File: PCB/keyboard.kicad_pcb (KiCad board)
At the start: 2 copper layers, 314.3 x 95.2 mm, 153 parts, among them J1 JST SH 4-pin, SW1 SW_Push, U1 ATmega32U4-A, U2 SRV05-4, Y1 16MHz

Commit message: Finished PCB designed, still not tested
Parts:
- added G***: LOGO, LOGO, F.Cu at (158.0, 316.7)
- added G***: LOGO, LOGO, F.Cu at (206.4, 315.9)
- moved C3 0.87 mm to (351.7, 268.5)
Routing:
- net GND: track 97.4 -> 132.0 mm
- net COL0: track 412.1 -> 416.8 mm
- net COL14: track 41.2 -> 43.5 mm
- net COL2: track 375.7 -> 377.1 mm
- net Net-(U1-XTAL1): track 9.71 -> 8.84 mm
- net D+: track 14.0 -> 13.4 mm
- net COL1: track 399.5 -> 399.4 mm, vias 2 -> 4
- net COL5: track 286.5 -> 286.4 mm, vias 2 -> 4
- added copper zone on B.Cu, net GND
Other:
- board text added: "1"
- board text added: "11.26.2022"
- board text added: "Designed by GAN!A"
- board text added: "Early, not yet tested version 0.1"
- board text added: "WD66 1st batch proto"
- board text added: "WD66 by 11Customs"

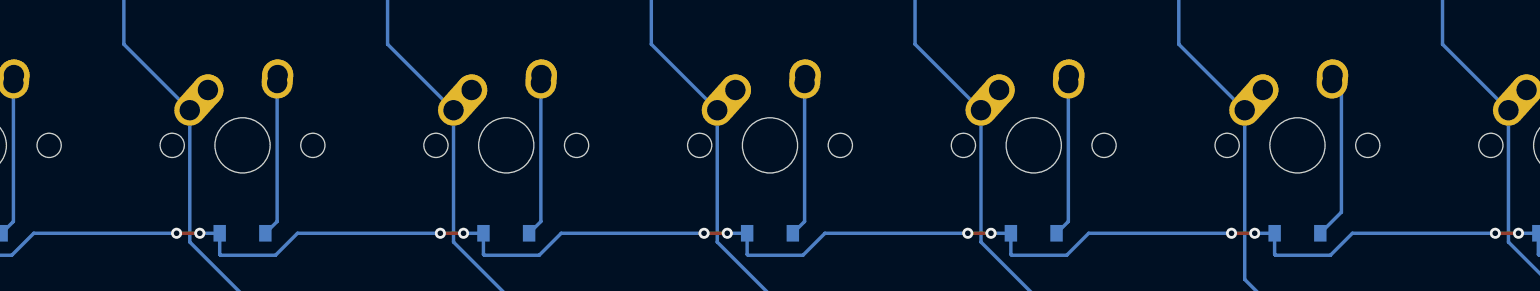
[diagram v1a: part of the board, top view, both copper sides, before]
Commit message: added holes for center standoffs
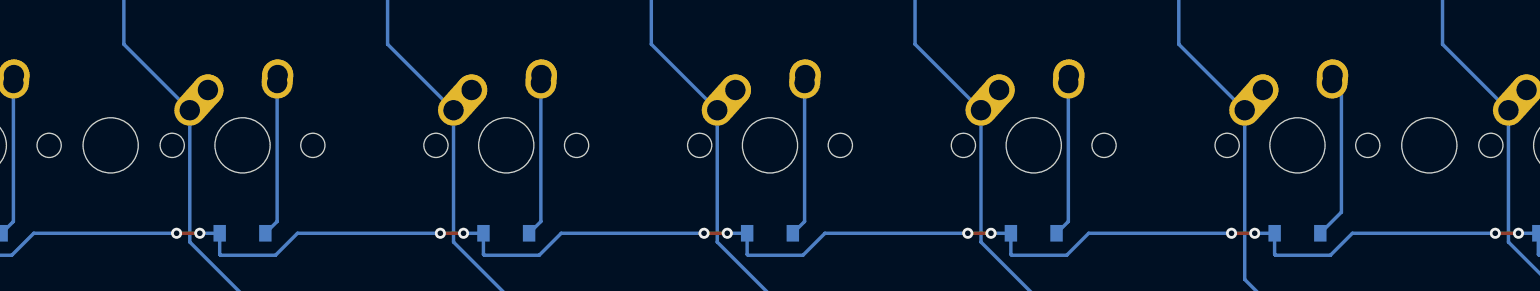
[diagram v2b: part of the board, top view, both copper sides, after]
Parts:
- added ?: , , F.Cu at (169.1, 278.6)
- added ?: , , F.Cu at (264.3, 278.6)
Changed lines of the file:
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@@
       (stroke (width 0.15) (type solid)) (layer "Dwgs.User"))
     (pad "" np_thru_hole circle locked (at -5.08 0 48.0996) (size 1.75 1.75) (drill 1.75) (layers *.Cu *.Mask))
-    (pad "" np_thru_hole circle locked (at 0 0) (size 3.9878 3.9878) (drill 3.9878) (layers *.Cu *.Mask))
+    (pad "" np_thru_hole circle locked (at 0 0) (size 3.9878 3.9878) (drill 3.9878) (layers F&B.Cu *.Mask))
     (pad "" np_thru_hole circle locked (at 5.08 0 48.0996) (size 1.75 1.75) (drill 1.75) (layers *.Cu *.Mask))
     (pad "1" thru_hole oval locked (at -3.81 -2.54 48.0996) (size 4.211556 2.25) (drill 1.47 (offset 0.980778 0)) (layers *.Cu "B.Mask")
@@
     (pad "2" thru_hole circle locked (at 2.54 -5.08) (size 2.25 2.25) (drill 1.47) (layers *.Cu "B.Mask")
       (net 48 "Net-(D28-A)") (pinfunction "ROW") (pintype "passive"))
+  )
+  (footprint "" (layer "F.Cu")
+    (at 169.06875 278.60625)
+    (fp_text reference "" (at 0 0) (layer "F.SilkS")
+      (effects (font (size 1.27 1.27) (thickness 0.15)))
+    )
+    (fp_text value "" (at 0 0) (layer "F.SilkS")
+      (effects (font (size 1.27 1.27) (thickness 0.15)))
+    )
+    (pad "" np_thru_hole circle locked (at 0 0) (size 3.9878 3.9878) (drill 3.9878) (layers F&B.Cu *.Mask))
   )
   (footprint "MX_Alps_Hybrid:MX-1U-NoLED" (layer "F.Cu")
@@
       (net 70 "Net-(D50-A)") (pinfunction "ROW") (pintype "passive"))
   )
+  (footprint "" (layer "F.Cu")
+    (at 264.31875 278.60625)
+    (fp_text reference "" (at 0 0) (layer "F.SilkS")
+      (effects (font (size 1.27 1.27) (thickness 0.15)))
+    )
+    (fp_text value "" (at 0 0) (layer "F.SilkS")
+      (effects (font (size 1.27 1.27) (thickness 0.15)))
+    )
+    (pad "" np_thru_hole circle locked (at 0 0) (size 3.9878 3.9878) (drill 3.9878) (layers F&B.Cu *.Mask))
+  )
   (footprint "MX_Alps_Hybrid:MX-1.5U-NoLED" (layer "F.Cu")

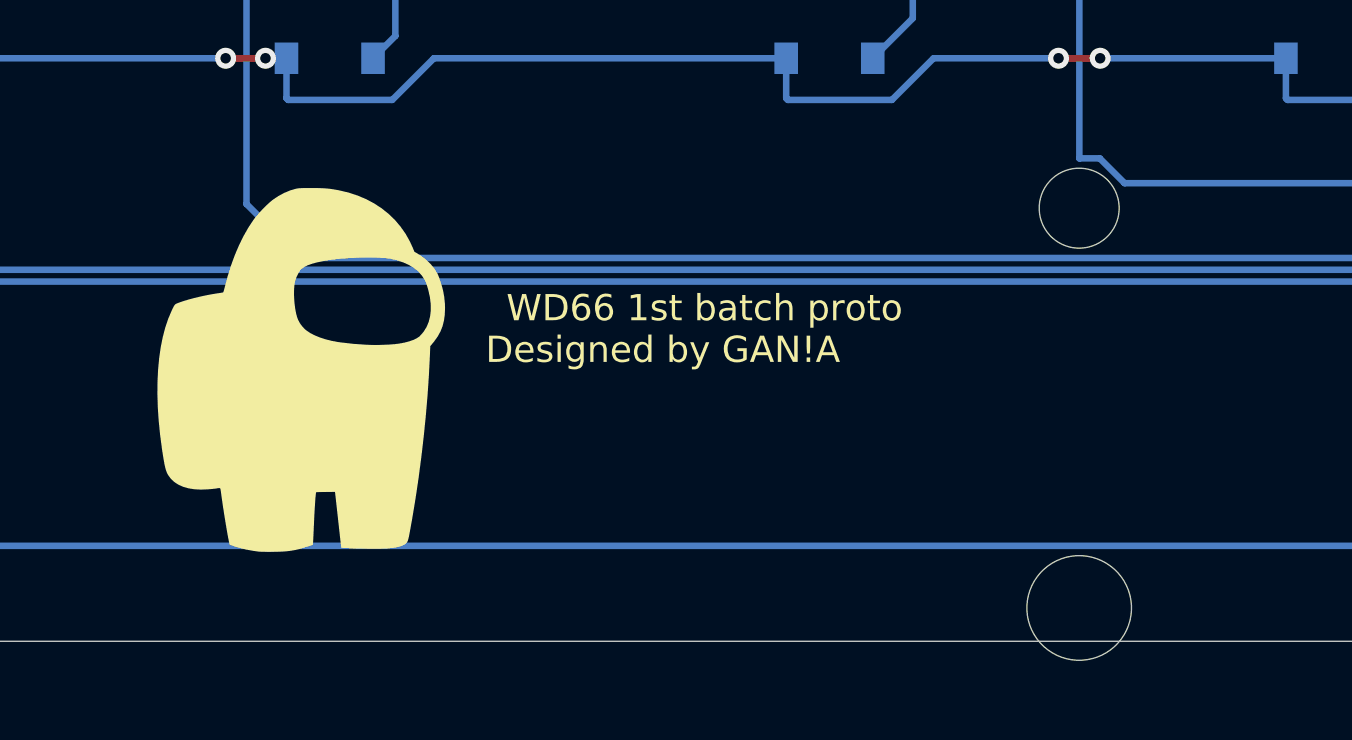
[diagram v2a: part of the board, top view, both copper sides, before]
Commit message: updated silkscreen
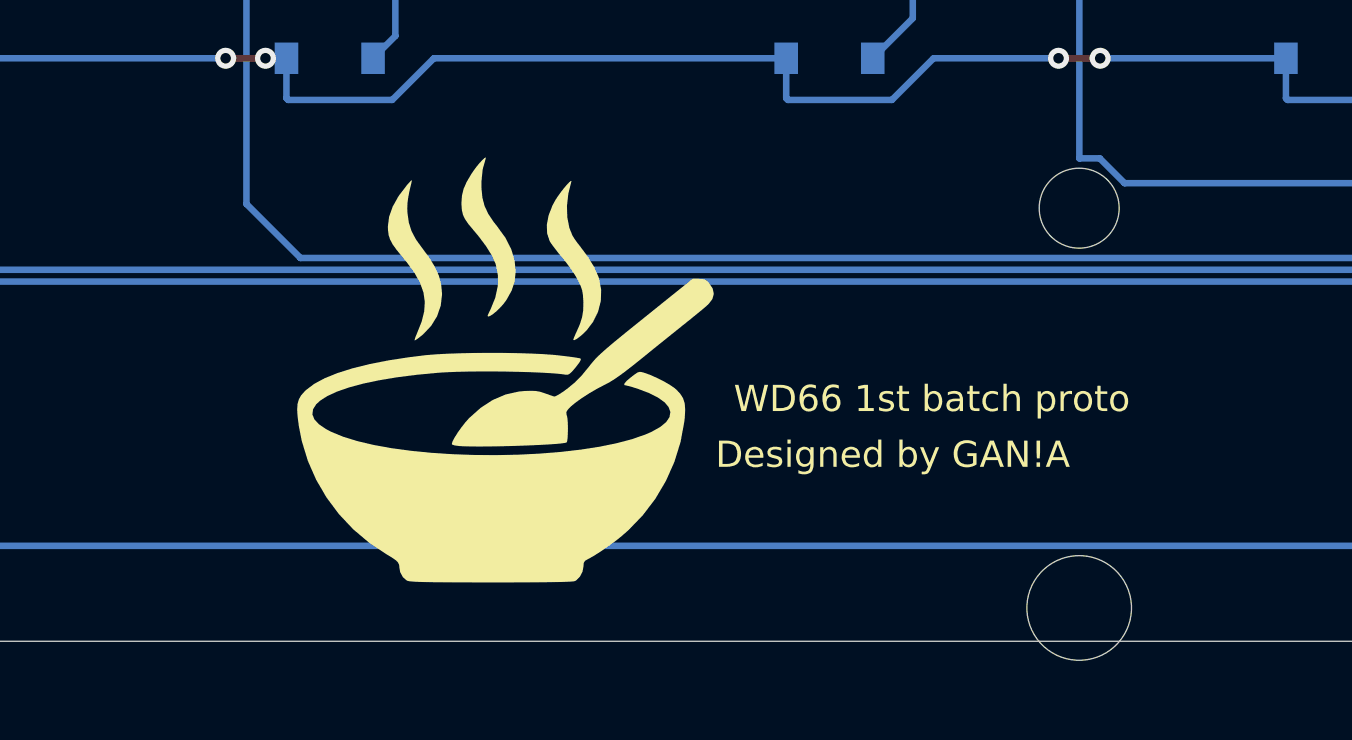
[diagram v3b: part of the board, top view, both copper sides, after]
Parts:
- moved G*** 7.49 mm to (213.9, 315.8)

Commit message: started redoing wiring
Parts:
- moved SW1 48.6 mm to (339.0, 240.5), turned to -90 degrees
- moved C7 35.4 mm to (337.4, 254.8), turned to -90 degrees
- moved R3 32.5 mm to (355.5, 250.9), turned to 0 degrees
- moved C6 32.3 mm to (347.9, 250.9), turned to 180 degrees
- moved C1 29.5 mm to (358.8, 249.9)
- moved C2 27.4 mm to (337.4, 265.9), turned to 90 degrees
- moved R4 21.9 mm to (340.6, 269.9), turned to 180 degrees
- moved U1 19.2 mm to (346.1, 261.0), turned to -90 degrees
- moved F1 18.1 mm to (345.3, 245.5)
- moved C4 18.0 mm to (355.6, 256.4), turned to 0 degrees
- moved R1 12.2 mm to (350.4, 246.8)
- moved R2 12.1 mm to (347.7, 246.8)
- moved U2 11.6 mm to (350.1, 242.1)
- moved J1 11.1 mm to (350.1, 235.7)
- moved Y1 10.6 mm to (355.6, 261.6), turned to 90 degrees
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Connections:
- U1 pad 18: COL0 -> unconnected-(U1-PD0)
- U1 pad 20: unconnected-(U1-PD2) -> COL0
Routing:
- net COL0: track 416.8 -> 0.50 mm, vias 6 -> 0
- net COL1: track 399.4 -> 0.99 mm, vias 4 -> 0
- net ROW0: track 379.2 -> 0.00 mm, vias 29 -> 0
- net COL2: track 377.1 -> 0.32 mm, vias 2 -> 0
- net COL4: track 377.6 -> 1.11 mm, vias 4 -> 0
- net ROW4: track 363.4 -> 0.00 mm, vias 2 -> 0
- net ROW1: track 350.4 -> 0.00 mm, vias 28 -> 0
- net ROW3: track 346.4 -> 0.00 mm, vias 20 -> 0
- net ROW2: track 343.5 -> 0.15 mm, vias 24 -> 0
- net COL3: track 320.1 -> 3.02 mm, vias 2 -> 0
- net COL5: track 286.4 -> 0.00 mm, vias 4 -> 0
- net COL6: track 259.7 -> 2.80 mm, vias 2 -> 0
- net COL7: track 237.6 -> 0.48 mm, vias 2 -> 0
- net COL9: track 214.1 -> 0.22 mm, vias 4 -> 0
- net COL8: track 210.6 -> 1.27 mm, vias 2 -> 0
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
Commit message: all new pretty wiring
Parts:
- removed the D13 at (121.4, 285.0)
- removed the D14 at (131.0, 304.0)
- added D65: D_Small, Diode_SMD:D_SOD-123, B.Cu at (364.2, 284.5)
- added D66: D_Small, Diode_SMD:D_SOD-123, B.Cu at (364.2, 304.0)
- moved D61 40.6 mm to (323.7, 285.0)
- moved D54 31.1 mm to (283.2, 304.0)
- moved D57 31.1 mm to (292.7, 285.0)
- moved D58 31.1 mm to (314.2, 304.0)
- moved D13 19.2 mm to (121.3, 285.0)
- moved D14 19.2 mm to (130.8, 304.0)
- moved D23 19.2 mm to (159.4, 285.0)
- moved D24 19.2 mm to (168.9, 304.0)
- moved D28 19.2 mm to (178.4, 285.0)
- moved D34 19.2 mm to (207.0, 304.0)
- moved D38 19.2 mm to (216.5, 285.0)
- moved D39 19.2 mm to (226.1, 304.0)
- moved D44 19.2 mm to (245.1, 304.0)
- moved D48 19.2 mm to (254.6, 285.0)
- moved D53 19.2 mm to (273.7, 285.0)
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- renumbered D18 to D13, D19 to D14, D23 to D18, D24 to D19, D28 to D23, D29 to D24, D33 to D28, D34 to D29, D38 to D33, D39 to D34, D43 to D38, D44 to D39, D48 to D43, D49 to D44, D53 to D48, D54 to D49, D57 to D53, D58 to D54, D61 to D57, D62 to D58, D65 to D61, D66 to D62
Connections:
- D13 pad 2: Net-(D18-A) -> Net-(D13-A)
- D14 pad 2: Net-(D19-A) -> Net-(D14-A)
- D18 pad 2: Net-(D23-A) -> Net-(D18-A)
- D19 pad 2: Net-(D24-A) -> Net-(D19-A)
- D23 pad 2: Net-(D28-A) -> Net-(D23-A)
- D24 pad 2: Net-(D29-A) -> Net-(D24-A)
- D28 pad 2: Net-(D33-A) -> Net-(D28-A)
- D29 pad 2: Net-(D34-A) -> Net-(D29-A)
- D33 pad 2: Net-(D38-A) -> Net-(D33-A)
- D34 pad 2: Net-(D39-A) -> Net-(D34-A)
- D38 pad 2: Net-(D43-A) -> Net-(D38-A)
- D39 pad 2: Net-(D44-A) -> Net-(D39-A)
- D43 pad 2: Net-(D48-A) -> Net-(D43-A)
- D44 pad 2: Net-(D49-A) -> Net-(D44-A)
- D48 pad 2: Net-(D53-A) -> Net-(D48-A)
- D49 pad 2: Net-(D54-A) -> Net-(D49-A)
- D53 pad 2: Net-(D57-A) -> Net-(D53-A)
- D54 pad 2: Net-(D58-A) -> Net-(D54-A)
- D57 pad 2: Net-(D61-A) -> Net-(D57-A)
- D58 pad 2: Net-(D62-A) -> Net-(D58-A)
- D61 pad 2: Net-(D65-A) -> Net-(D61-A)
- D62 pad 2: Net-(D66-A) -> Net-(D62-A)
- MX13 pad 1: COL2 -> COL3
- MX14 pad 1: COL2 -> COL3
- MX18 pad 1: COL3 -> COL4
- MX19 pad 1: COL3 -> COL4
- MX20 pad 1: COL3 -> COL6
- MX23 pad 1: COL4 -> COL5
- MX24 pad 1: COL4 -> COL5
- MX25 pad 1: COL4 -> COL9
- MX28 pad 1: COL5 -> COL6
- MX29 pad 1: COL5 -> COL6
- MX30 pad 1: COL5 -> COL10
- MX33 pad 1: COL6 -> COL7
- MX34 pad 1: COL6 -> COL7
- MX35 pad 1: COL6 -> COL11
- MX38 pad 1: COL7 -> COL8
- MX39 pad 1: COL7 -> COL8
- MX40 pad 1: COL7 -> COL12
- MX43 pad 1: COL8 -> COL9
- MX44 pad 1: COL8 -> COL9
- MX45 pad 1: COL8 -> COL13
- MX48 pad 1: COL9 -> COL10
- MX49 pad 1: COL9 -> COL10
- MX50 pad 1: COL9 -> COL14
- MX53 pad 1: COL10 -> COL11
- MX54 pad 1: COL10 -> COL11
- MX57 pad 1: COL11 -> COL12
- MX58 pad 1: COL11 -> COL12
- MX61 pad 1: COL12 -> COL13
- MX62 pad 1: COL12 -> COL13
- MX65 pad 1: COL13 -> COL14
- MX65 pad 2: Net-(D65-A) -> Net-(MX65-ROW)
- MX66 pad 1: COL13 -> COL14
- MX66 pad 2: Net-(D66-A) -> Net-(MX66-ROW)
- MX8 pad 1: COL1 -> COL2
- MX9 pad 1: COL1 -> COL2
- U1 pad 1: COL11 -> ROW0
- U1 pad 10: COL2 -> ROW2
- U1 pad 11: COL1 -> ROW1
- U1 pad 12: COL12 -> COL14
- U1 pad 20: COL0 -> unconnected-(U1-PD2)
- U1 pad 21: COL14 -> unconnected-(U1-PD3)
- U1 pad 22: COL13 -> unconnected-(U1-PD5)
- U1 pad 25: ROW0 -> COL0
- U1 pad 26: ROW1 -> COL1
- U1 pad 27: ROW2 -> COL2
- U1 pad 28: ROW3 -> COL3
- U1 pad 29: ROW4 -> COL4
- U1 pad 30: unconnected-(U1-PB6) -> COL5
- U1 pad 31: unconnected-(U1-PC6) -> COL6
- U1 pad 32: unconnected-(U1-PC7) -> COL7
- U1 pad 36: COL5 -> COL8
- U1 pad 37: COL6 -> COL9
- U1 pad 38: COL7 -> COL10
- U1 pad 39: COL8 -> COL11
- U1 pad 40: COL9 -> COL12
- U1 pad 41: COL10 -> COL13
- U1 pad 8: COL4 -> ROW4
- U1 pad 9: COL3 -> ROW3
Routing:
- net ROW4: track 0.00 -> 422.4 mm
- net ROW3: track 0.00 -> 396.8 mm
- net COL0: track 0.50 -> 383.7 mm, vias 0 -> 3
- net ROW2: track 0.15 -> 380.3 mm
- net ROW1: track 0.00 -> 366.5 mm, vias 0 -> 2
- net COL1: track 0.99 -> 361.7 mm, vias 0 -> 3
- net COL2: track 0.32 -> 351.1 mm, vias 0 -> 3
- net ROW0: track 0.00 -> 330.1 mm, vias 0 -> 2
- net COL3: track 3.02 -> 307.7 mm, vias 0 -> 1
- net COL4: track 1.11 -> 289.8 mm, vias 0 -> 1
- net COL5: track 0.00 -> 267.2 mm, vias 0 -> 1
- net COL6: track 2.80 -> 268.6 mm, vias 0 -> 1
- net COL7: track 0.48 -> 225.5 mm, vias 0 -> 1
- net COL9: track 0.22 -> 202.8 mm, vias 0 -> 1
- net COL8: track 1.27 -> 196.2 mm, vias 0 -> 1
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- added copper zone on F.Cu, net GND
